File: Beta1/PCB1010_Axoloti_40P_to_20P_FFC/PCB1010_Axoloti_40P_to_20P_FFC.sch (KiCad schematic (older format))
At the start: 22 parts, among them J1 Axoloti_40Pin, J2 FPC_20POS

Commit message: Updated connector pinouts. Ready for Fab
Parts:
- removed GND1, VCC1: CONN_01X01, Liberry:single_0.1, symbol CONN_01X01
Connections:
- net labels removed: !OLED_RESET
- wire segments 62 -> 59
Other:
- note added: "PC2\n"
- note added: "PC3"
- note added: "PC4"
- moved on the sheet: ANALOG_OUT0, CS_0_7, CS_8_15, GND0, I2C_SCL0, I2C_SDA0, J2, JOY0_SW0, JOY0_X0, JOY0_Y0, PC0, PC1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

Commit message: Added TH connector, updated board outline
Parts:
- added J3: FPC_20POS, Liberry:FFC_20x1mm_SLW20R-1C7LF, symbol FPC_20POS
- added R? (x4): 0, Resistors_SMD:R_0603, symbol R
- added U?: STM32F103C8T6_BLUE_PILL, symbol STM32F103C8T6_BLUE_PILL
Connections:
- net labels added: CS_0_7_AXO, CS_0_7_EXT, CS_8_15_AXO, CS_8_15_EXT, I2C_SCL_AXO, I2C_SCL_EXT, I2C_SDA_AXO, I2C_SDA_EXT, RESET, RX_AXO, RX_EXT, SPI_CLK_AXO, SPI_CLK_EXT, SPI_MISO_AXO, SPI_MISO_EXT, SPI_MOSI_AXO, SPI_MOSI_EXT, TX_AXO, TX_EXT, UART_RX_EXT, UART_TX_EXT
- net labels removed: CS_0_7, CS_8_15, I2C_SCL, I2C_SDA, RX, SPI_CLK, SPI_MISO, SPI_MOSI, TX
- wire segments 59 -> 124
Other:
- note added: "52271-1679\n20 pos FFC x 1 mm\nSMD"
- note added: "SLW20R-1C7LF\n20 pos FFC x 1mm\nTH"
- moved on the sheet: J1

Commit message: Added Bluepill to PCB1010 design. Layout complete. Ready to route.
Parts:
- removed ANALOG_OUT0, CS_0_7, CS_8_15, GND0, I2C_SCL0, I2C_SDA0, JOY0_SW0, JOY0_X0, JOY0_Y0, PC0, PC1, RX0, SPI_CLK0, SPI_MISO0, SPI_MOSI0, TX0, VCC0, VOLUME0: CONN_01X01, Liberry:single_0.1, symbol CONN_01X01
- U5000: renamed from U?; footprint (none) -> Liberry:BLUEPILL_CORTEXM3_STM32F103C8T6_THIN
- gave numbers to parts that had none: 4
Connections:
- net labels added: PC0_AXO, PC0_EXT, PC1_AXO, PC1_EXT
- net labels removed: PC0, PC1
- wire segments 124 -> 126

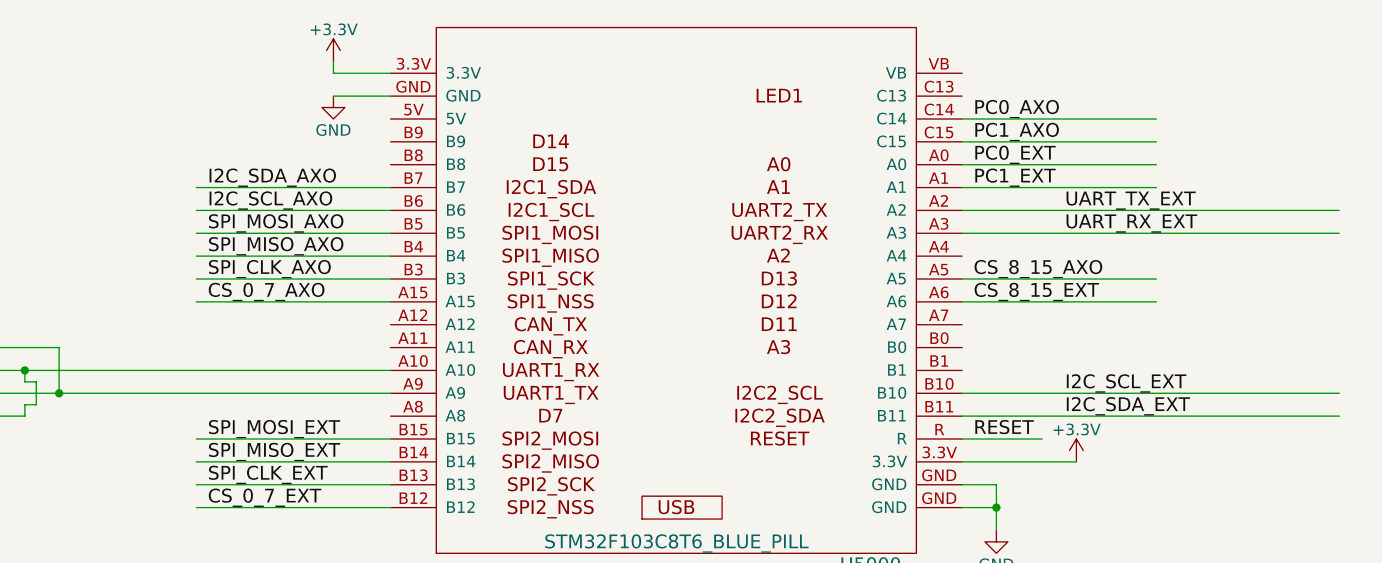
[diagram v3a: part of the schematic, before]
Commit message: Corrected serial UART RX/TX nets
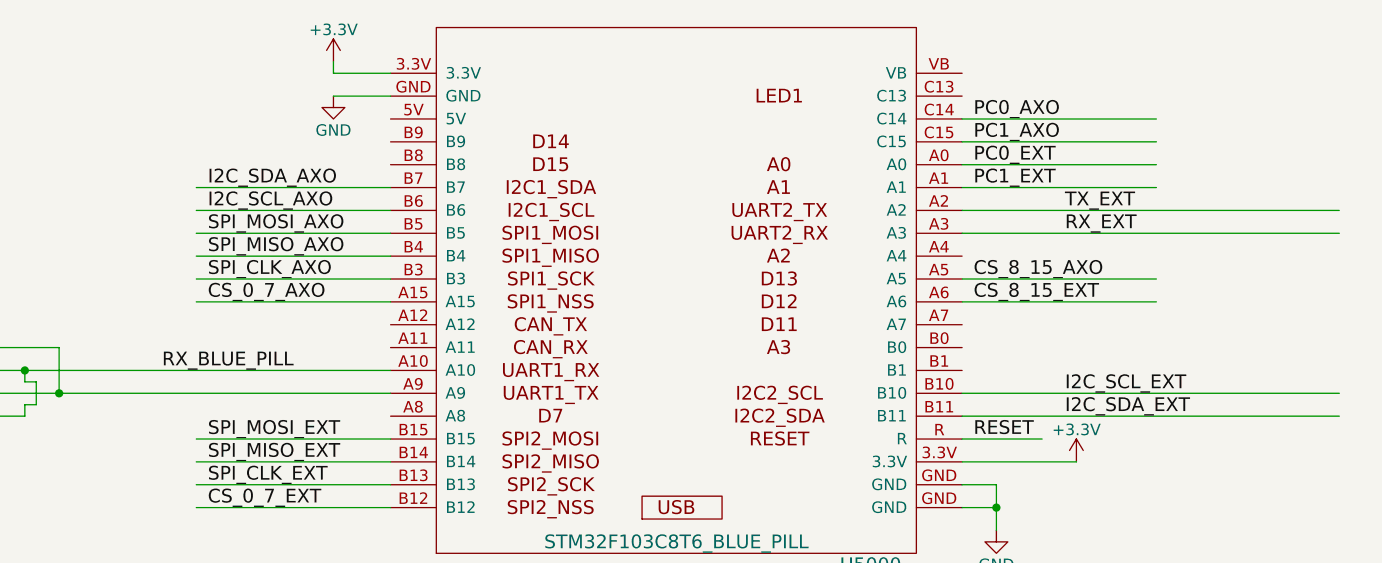
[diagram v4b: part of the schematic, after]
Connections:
- net labels added: RX_BLUE_PILL
- net labels removed: UART_RX_EXT, UART_TX_EXT
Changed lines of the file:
@@
 $EndComp
 Text Label 13600 2850 0    60   ~ 0
-UART_RX_EXT
+RX_EXT
 Text Label 13600 2750 0    60   ~ 0
-UART_TX_EXT
+TX_EXT
 Text Label 13600 3650 0    60   ~ 0
 I2C_SDA_EXT
@@
 Wire Wire Line
 	13150 2650 14000 2650
+Text Label 9650 3450 0    60   ~ 0
+RX_BLUE_PILL
 $EndSCHEMATC

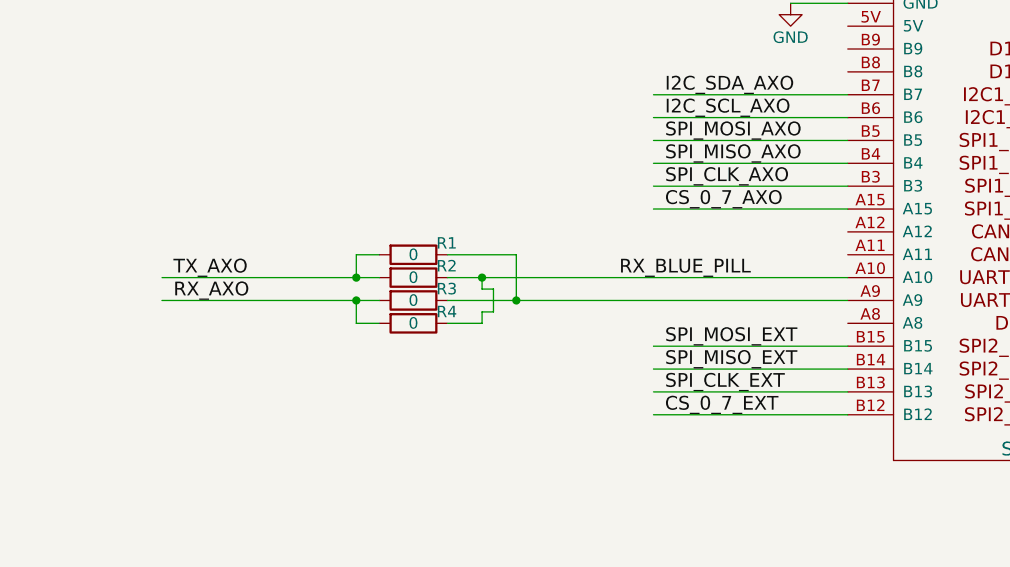
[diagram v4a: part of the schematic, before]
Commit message: Updated FFC footprint, Removed proto resistors, deleted all traces
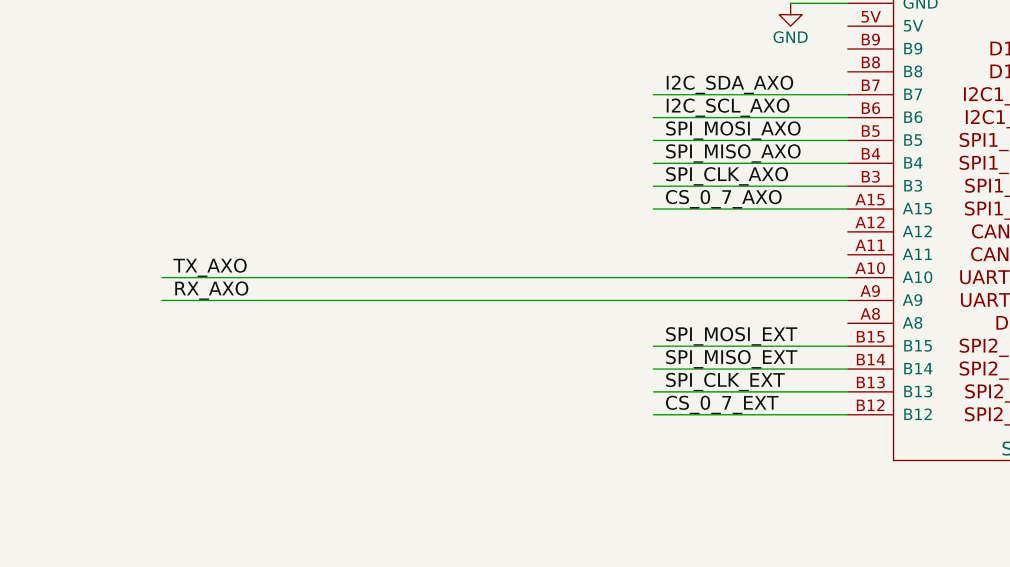
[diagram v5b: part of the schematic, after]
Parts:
- removed R1, R2, R3, R4: 0, Resistors_SMD:R_0603, symbol R
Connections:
- net labels removed: RX_BLUE_PILL
- wire segments 126 -> 112
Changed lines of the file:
@@
 Text Label 13200 2350 0    60   ~ 0
 PC0_AXO
-$Comp
-L R R2
-U 1 1 5AA0BFBD
-P 8750 3450
-F 0 "R2" V 8700 3550 50  0000 L CNN
-F 1 "0" V 8750 3450 50  0000 C CNN
-F 2 "Resistors_SMD:R_0603" V 8680 3450 50  0001 C CNN
-F 3 "" H 8750 3450 50  0000 C CNN
-F 4 "VISHAY" V 8750 3450 60  0001 C CNN "MFG"
-F 5 "CRCW06030000ZSTA" V 8650 3500 60  0001 C CNN "MPN"
-	1    8750 3450
-	0    1    1    0
-$EndComp
-$Comp
-L R R3
-U 1 1 5AA0CBD8
-P 8750 3550
-F 0 "R3" V 8700 3650 50  0000 L CNN
-F 1 "0" V 8750 3550 50  0000 C CNN
-F 2 "Resistors_SMD:R_0603" V 8680 3550 50  0001 C CNN
-F 3 "" H 8750 3550 50  0000 C CNN
-F 4 "VISHAY" V 8750 3550 60  0001 C CNN "MFG"
-F 5 "CRCW06030000ZSTA" V 8650 3600 60  0001 C CNN "MPN"
-	1    8750 3550
-	0    1    1    0
-$EndComp
-$Comp
-L R R1
-U 1 1 5AA0CD94
-P 8750 3350
-F 0 "R1" V 8700 3450 50  0000 L CNN
-F 1 "0" V 8750 3350 50  0000 C CNN
-F 2 "Resistors_SMD:R_0603" V 8680 3350 50  0001 C CNN
-F 3 "" H 8750 3350 50  0000 C CNN
-F 4 "VISHAY" V 8750 3350 60  0001 C CNN "MFG"
-F 5 "CRCW06030000ZSTA" V 8650 3400 60  0001 C CNN "MPN"
-	1    8750 3350
-	0    1    1    0
-$EndComp
-$Comp
-L R R4
-U 1 1 5AA0D0A0
-P 8750 3650
-F 0 "R4" V 8700 3750 50  0000 L CNN
-F 1 "0" V 8750 3650 50  0000 C CNN
-F 2 "Resistors_SMD:R_0603" V 8680 3650 50  0001 C CNN
-F 3 "" H 8750 3650 50  0000 C CNN
-F 4 "VISHAY" V 8750 3650 60  0001 C CNN "MFG"
-F 5 "CRCW06030000ZSTA" V 8650 3700 60  0001 C CNN "MPN"
-	1    8750 3650
-	0    1    1    0
-$EndComp
 Text Label 13600 2850 0    60   ~ 0
 RX_EXT
@@
 	13150 3050 14000 3050
 Wire Wire Line
-	7650 3450 8600 3450
-Wire Wire Line
-	7650 3550 8600 3550
-Wire Wire Line
-	8600 3350 8500 3350
-Wire Wire Line
-	8500 3350 8500 3450
-Connection ~ 8500 3450
-Wire Wire Line
-	8500 3550 8500 3650
-Wire Wire Line
-	8500 3650 8600 3650
-Connection ~ 8500 3550
-Wire Wire Line
-	8900 3450 10650 3450
-Wire Wire Line
-	8900 3350 9200 3350
-Wire Wire Line
-	9200 3350 9200 3550
-Wire Wire Line
-	8900 3550 10650 3550
-Connection ~ 9200 3550
-Wire Wire Line
-	8900 3650 9050 3650
-Wire Wire Line
-	9050 3650 9050 3600
-Wire Wire Line
-	9050 3600 9100 3600
-Wire Wire Line
-	9100 3600 9100 3500
-Wire Wire Line
-	9100 3500 9050 3500
-Wire Wire Line
-	9050 3500 9050 3450
-Connection ~ 9050 3450
+	7650 3450 10650 3450
+Wire Wire Line
+	7650 3550 10650 3550
 Wire Wire Line
 	13150 2850 14800 2850
@@
 Wire Wire Line
 	13150 2650 14000 2650
-Text Label 9650 3450 0    60   ~ 0
-RX_BLUE_PILL
 $EndSCHEMATC

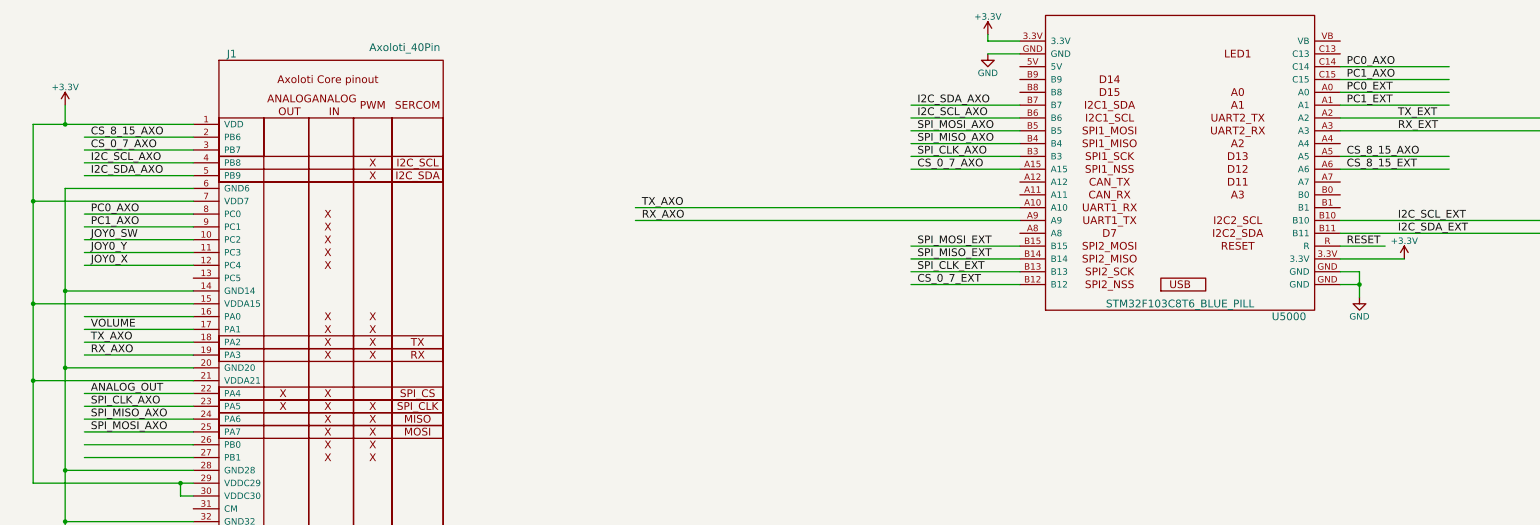
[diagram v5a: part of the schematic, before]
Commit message: Removed signals from STM32 that weren't being changed.
Removed SPI and control signals
Removed PC0, PC1
Signals now go directly from axoloti to PCB1005
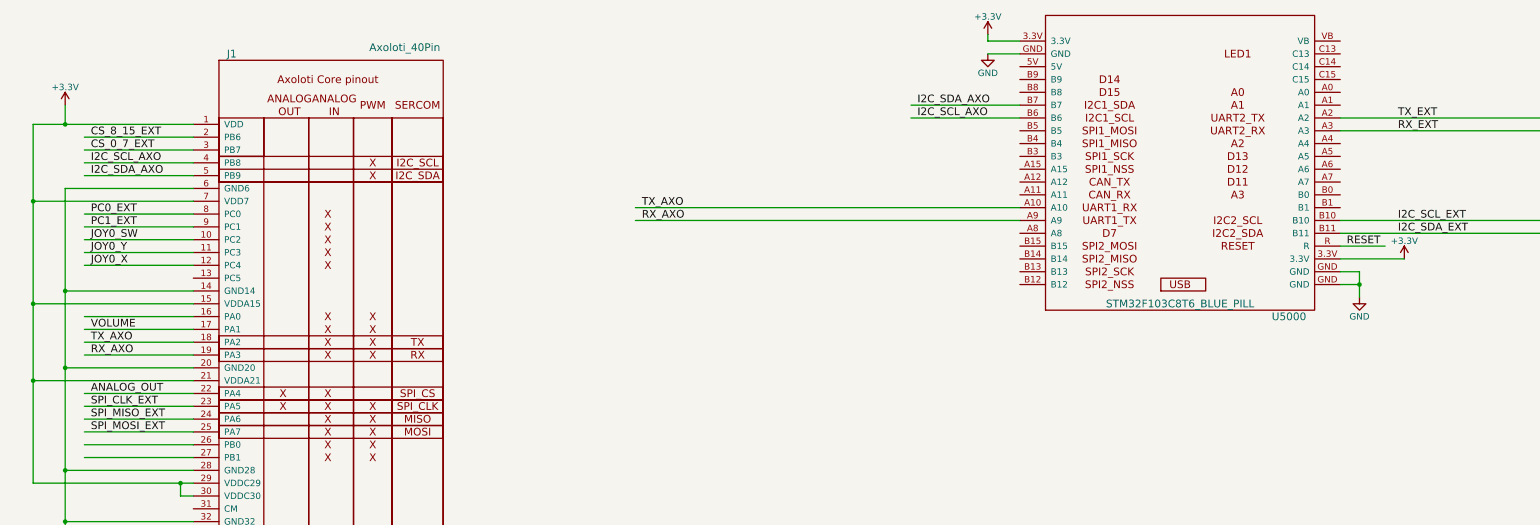
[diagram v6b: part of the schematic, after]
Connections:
- net labels removed: CS_0_7_AXO, CS_8_15_AXO, PC0_AXO, PC1_AXO, SPI_CLK_AXO, SPI_MISO_AXO, SPI_MOSI_AXO
- wire segments 112 -> 98
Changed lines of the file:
@@
 $EndComp
 Text Label 3400 5200 0    60   ~ 0
-SPI_MOSI_AXO
+SPI_MOSI_EXT
 Text Label 3400 5100 0    60   ~ 0
-SPI_MISO_AXO
+SPI_MISO_EXT
 Text Label 3400 5000 0    60   ~ 0
-SPI_CLK_AXO
+SPI_CLK_EXT
 Text Label 3400 3000 0    60   ~ 0
-CS_0_7_AXO
+CS_0_7_EXT
 Text Label 3400 2900 0    60   ~ 0
-CS_8_15_AXO
+CS_8_15_EXT
 $Comp
 L +3.3V #PWR02
@@
 ANALOG_OUT
 Text Label 3400 3600 0    60   ~ 0
-PC1_AXO
+PC1_EXT
 Text Label 20300 3100 0    60   ~ 0
 PC0_EXT
@@
 PC1_EXT
 Text Label 3400 3500 0    60   ~ 0
-PC0_AXO
+PC0_EXT
 Text Notes 19750 3300 0    60   ~ 0
 PC2\n
@@
 Text Label 9850 2650 0    60   ~ 0
 I2C_SDA_AXO
-Text Label 9850 2850 0    60   ~ 0
-SPI_MOSI_AXO
-Text Label 9850 2950 0    60   ~ 0
-SPI_MISO_AXO
-Text Label 9850 3050 0    60   ~ 0
-SPI_CLK_AXO
-Text Label 9850 3150 0    60   ~ 0
-CS_0_7_AXO
-Text Label 13200 3050 0    60   ~ 0
-CS_8_15_AXO
 Text Label 7700 3450 0    60   ~ 0
 TX_AXO
 Text Label 7700 3550 0    60   ~ 0
 RX_AXO
-Text Label 13200 2450 0    60   ~ 0
-PC1_AXO
-Text Label 13200 2350 0    60   ~ 0
-PC0_AXO
 Text Label 13600 2850 0    60   ~ 0
 RX_EXT
@@
 Text Label 13600 3550 0    60   ~ 0
 I2C_SCL_EXT
-Text Label 9850 3750 0    60   ~ 0
-SPI_MOSI_EXT
-Text Label 9850 3850 0    60   ~ 0
-SPI_MISO_EXT
-Text Label 9850 3950 0    60   ~ 0
-SPI_CLK_EXT
 Wire Wire Line
 	3350 3200 4200 3200
@@
 	9800 2750 10650 2750
 Wire Wire Line
-	9800 3050 10650 3050
-Wire Wire Line
-	9800 2950 10650 2950
-Wire Wire Line
-	9800 2850 10650 2850
-Wire Wire Line
-	13150 2350 14000 2350
-Wire Wire Line
-	13150 2450 14000 2450
-Wire Wire Line
-	9800 3150 10650 3150
-Wire Wire Line
-	13150 3050 14000 3050
-Wire Wire Line
 	7650 3450 10650 3450
 Wire Wire Line
@@
 Wire Wire Line
 	13150 3550 14800 3550
-Wire Wire Line
-	9800 3950 10650 3950
-Wire Wire Line
-	9800 3850 10650 3850
-Wire Wire Line
-	9800 3750 10650 3750
-Text Label 9850 4050 0    60   ~ 0
-CS_0_7_EXT
-Wire Wire Line
-	9800 4050 10650 4050
-Text Label 13200 3150 0    60   ~ 0
-CS_8_15_EXT
-Wire Wire Line
-	13150 3150 14000 3150
 $Comp
 L +3.3V #PWR07
@@
 Wire Wire Line
 	10650 2250 10400 2250
-Text Label 13200 2650 0    60   ~ 0
-PC1_EXT
-Text Label 13200 2550 0    60   ~ 0
-PC0_EXT
-Wire Wire Line
-	13150 2550 14000 2550
-Wire Wire Line
-	13150 2650 14000 2650
 $EndSCHEMATC

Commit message: Rough placement
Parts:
- J1: symbol Axoloti_40Pin -> PCB1010_Axoloti_40P_to_20P_FFC-rescue:Axoloti_40Pin
- J2, J3: symbol FPC_20POS -> PCB1010_Axoloti_40P_to_20P_FFC-rescue:FPC_20POS
- U5000: symbol STM32F103C8T6_BLUE_PILL -> PCB1010_Axoloti_40P_to_20P_FFC-rescue:STM32F103C8T6_BLUE_PILL
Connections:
- wire segments 98 -> 115
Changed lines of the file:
@@
-EESchema Schematic File Version 2
-LIBS:74xgxx
-LIBS:74xx
-LIBS:ac-dc
-LIBS:actel
-LIBS:adc-dac
-LIBS:Altera
-LIBS:analog_devices
-LIBS:analog_switches
-LIBS:atmel
-LIBS:audio
-LIBS:battery_management
-LIBS:bbd
-LIBS:brooktre
-LIBS:cmos_ieee
-LIBS:cmos4000
-LIBS:conn
-LIBS:contrib
-LIBS:cypress
-LIBS:dc-dc
-LIBS:device
-LIBS:digital-audio
-LIBS:diode
-LIBS:display
-LIBS:dsp
-LIBS:elec-unifil
-LIBS:ESD_Protection
-LIBS:ftdi
-LIBS:gennum
-LIBS:graphic
-LIBS:hc11
-LIBS:intel
-LIBS:interface
-LIBS:ir
-LIBS:Lattice
-LIBS:linear
-LIBS:logo
-LIBS:maxim
-LIBS:memory
-LIBS:microchip
-LIBS:microchip_dspic33dsc
-LIBS:microchip_pic10mcu
-LIBS:microchip_pic12mcu
-LIBS:microchip_pic16mcu
-LIBS:microchip_pic18mcu
-LIBS:microchip_pic32mcu
-LIBS:microcontrollers
-LIBS:motor_drivers
-LIBS:motorola
-LIBS:msp430
-LIBS:nordicsemi
-LIBS:nxp_armmcu
-LIBS:onsemi
-LIBS:opto
-LIBS:Oscillators
-LIBS:philips
-LIBS:power
-LIBS:Power_Management
-LIBS:powerint
-LIBS:pspice
-LIBS:references
-LIBS:regul
-LIBS:relays
-LIBS:rfcom
-LIBS:sensors
-LIBS:silabs
-LIBS:siliconi
-LIBS:stm8
-LIBS:stm32
-LIBS:supertex
-LIBS:switches
-LIBS:texas
-LIBS:transf
-LIBS:transistors
-LIBS:ttl_ieee
-LIBS:valves
-LIBS:video
-LIBS:Worldsemi
-LIBS:Xicor
-LIBS:xilinx
-LIBS:Zilog
-LIBS:believotron_wanderlust
+EESchema Schematic File Version 4
 LIBS:PCB1010_Axoloti_40P_to_20P_FFC-cache
-EELAYER 25 0
+EELAYER 26 0
 EELAYER END
 $Descr D 34000 22000
@@
 Date
 $Comp
-L Axoloti_40Pin J1
+L PCB1010_Axoloti_40P_to_20P_FFC-rescue:Axoloti_40Pin J1
 U 1 1 591BA4F8
 P 4200 7750
@@
 I2C_SDA_AXO
 $Comp
-L GND #PWR01
+L PCB1010_Axoloti_40P_to_20P_FFC-rescue:GND #PWR01
 U 1 1 591BA513
 P 3200 7000
@@
 CS_8_15_EXT
 $Comp
-L +3.3V #PWR02
+L PCB1010_Axoloti_40P_to_20P_FFC-rescue:+3.3V #PWR02
 U 1 1 591E099F
 P 3200 2650
@@
 RX_AXO
 $Comp
-L +3.3V #PWR03
+L PCB1010_Axoloti_40P_to_20P_FFC-rescue:+3.3V #PWR03
 U 1 1 596EA01A
 P 21000 2650
@@
 $EndComp
 $Comp
-L GND #PWR04
+L PCB1010_Axoloti_40P_to_20P_FFC-rescue:GND #PWR04
 U 1 1 596EA0DD
 P 21050 4900
@@
 $EndComp
 $Comp
-L FPC_20POS J2
+L PCB1010_Axoloti_40P_to_20P_FFC-rescue:FPC_20POS J2
 U 1 1 596EA301
 P 21400 2800
@@
 SPI_MISO_EXT
 $Comp
-L +3.3V #PWR05
+L PCB1010_Axoloti_40P_to_20P_FFC-rescue:+3.3V #PWR05
 U 1 1 5AA080DB
 P 24350 2700
@@
 $EndComp
 $Comp
-L GND #PWR06
+L PCB1010_Axoloti_40P_to_20P_FFC-rescue:GND #PWR06
 U 1 1 5AA080E1
 P 24400 4950
@@
 $EndComp
 $Comp
-L FPC_20POS J3
+L PCB1010_Axoloti_40P_to_20P_FFC-rescue:FPC_20POS J3
 U 1 1 5AA080E7
 P 24750 2850
@@
 52271-1679\n20 pos FFC x 1 mm\nSMD
 $Comp
-L STM32F103C8T6_BLUE_PILL U5000
+L PCB1010_Axoloti_40P_to_20P_FFC-rescue:STM32F103C8T6_BLUE_PILL U5000
 U 1 1 5AA095FF
 P 11950 3100
@@
 	3350 3100 4200 3100
 Wire Wire Line
-	2950 2800 4200 2800
-Wire Wire Line
-	3200 3300 3200 7000
+	2950 2800 3200 2800
+Wire Wire Line
+	3200 3300 3200 4100
 Wire Wire Line
 	3200 6000 4200 6000
@@
 	2950 4800 4200 4800
 Wire Wire Line
-	2950 5600 4200 5600
+	2950 5600 4100 5600
 Wire Wire Line
 	4200 5700 4100 5700
@@
 	4200 3700 3350 3700
 Wire Wire Line
-	2950 2800 2950 5600
+	2950 2800 2950 3400
 Connection ~ 3200 2800
 Connection ~ 2950 3400
@@
 	21200 2800 21000 2800
 Wire Wire Line
-	21000 2650 21000 2900
+	21000 2650 21000 2800
 Connection ~ 21000 2800
 Wire Wire Line
 	21200 4600 21050 4600
 Wire Wire Line
-	21050 4600 21050 4900
-Wire Wire Line
-	19450 4700 21200 4700
+	21050 4600 21050 4700
+Wire Wire Line
+	19450 4700 21050 4700
 Connection ~ 21050 4700
 Wire Wire Line
@@
 Connection ~ 21000 2900
 Wire Wire Line
-	19550 2900 21200 2900
+	19550 2900 21000 2900
 Wire Wire Line
 	22800 4250 24550 4250
@@
 	24550 2850 24350 2850
 Wire Wire Line
-	24350 2700 24350 2950
+	24350 2700 24350 2850
 Connection ~ 24350 2850
 Wire Wire Line
 	24550 4650 24400 4650
 Wire Wire Line
-	24400 4650 24400 4950
+	24400 4650 24400 4750
 Connection ~ 24400 4750
 Wire Wire Line
@@
 Wire Wire Line
 	22800 3250 24550 3250
-Connection ~ 24350 2950
 Wire Wire Line
 	24550 4750 24400 4750
@@
 	13150 3550 14800 3550
 $Comp
-L +3.3V #PWR07
+L PCB1010_Axoloti_40P_to_20P_FFC-rescue:+3.3V #PWR07
 U 1 1 5AA19E22
 P 10400 2100
@@
 $EndComp
 $Comp
-L +3.3V #PWR08
+L PCB1010_Axoloti_40P_to_20P_FFC-rescue:+3.3V #PWR08
 U 1 1 5AA19FB3
 P 13650 3850
@@
 RESET
 $Comp
-L GND #PWR09
+L PCB1010_Axoloti_40P_to_20P_FFC-rescue:GND #PWR09
 U 1 1 5AA1BEA8
 P 13300 4150
@@
 	13150 3950 13300 3950
 Wire Wire Line
-	13300 3950 13300 4150
+	13300 3950 13300 4050
 Wire Wire Line
 	13150 4050 13300 4050
@@
 	10400 2150 10650 2150
 $Comp
-L GND #PWR010
+L PCB1010_Axoloti_40P_to_20P_FFC-rescue:GND #PWR010
 U 1 1 5AA1D02A
 P 10400 2250
@@
 Wire Wire Line
 	10650 2250 10400 2250
+Wire Wire Line
+	3200 6000 3200 7000
+Wire Wire Line
+	3200 5900 3200 6000
+Wire Wire Line
+	3200 5500 3200 5900
+Wire Wire Line
+	3200 4700 3200 5500
+Wire Wire Line
+	3200 4100 3200 4700
+Wire Wire Line
+	4100 5600 4200 5600
+Wire Wire Line
+	3200 2800 4200 2800
+Wire Wire Line
+	2950 3400 2950 4200
+Wire Wire Line
+	2950 4200 2950 4800
+Wire Wire Line
+	2950 4800 2950 5600
+Wire Wire Line
+	21000 2800 21000 2900
+Wire Wire Line
+	21050 4700 21050 4900
+Wire Wire Line
+	21050 4700 21200 4700
+Wire Wire Line
+	21000 2900 21200 2900
+Wire Wire Line
+	24350 2850 24350 2950
+Wire Wire Line
+	24400 4750 24400 4950
+Wire Wire Line
+	13300 4050 13300 4150
 $EndSCHEMATC
